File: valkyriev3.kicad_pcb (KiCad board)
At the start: 4 copper layers, 70 x 100 mm, 119 parts, among them J1 USB_C_Receptacle_USB2.0_16P, J10 Conn_01x03, J11 Conn_01x03, J2 DE9_Pins_MountingHoles, J3 SMA_180C, J4 SMA_180C, J5 Conn_01x02_Socket, J6 Conn_01x02_Socket, J7 Conn_01x02_Socket, J8 Conn_01x03, J9 Conn_01x05, Q1 BC817, Q2 BC817, Q3 BC817, Q4 BC817, Q5 BC817, Q6 DMG3420U, Q7 DMP2305U, Q8 DMG3420U, SW1 SW_SPST, SW2 SW_SPST, U1 W25Q128JVS, U10 LPS22HB, U2 ESP32-S3-MINI-1U, U3 MAX3232, U4 AMS1117-3.3, U5 TPS562202, U9 MS5607-02BA

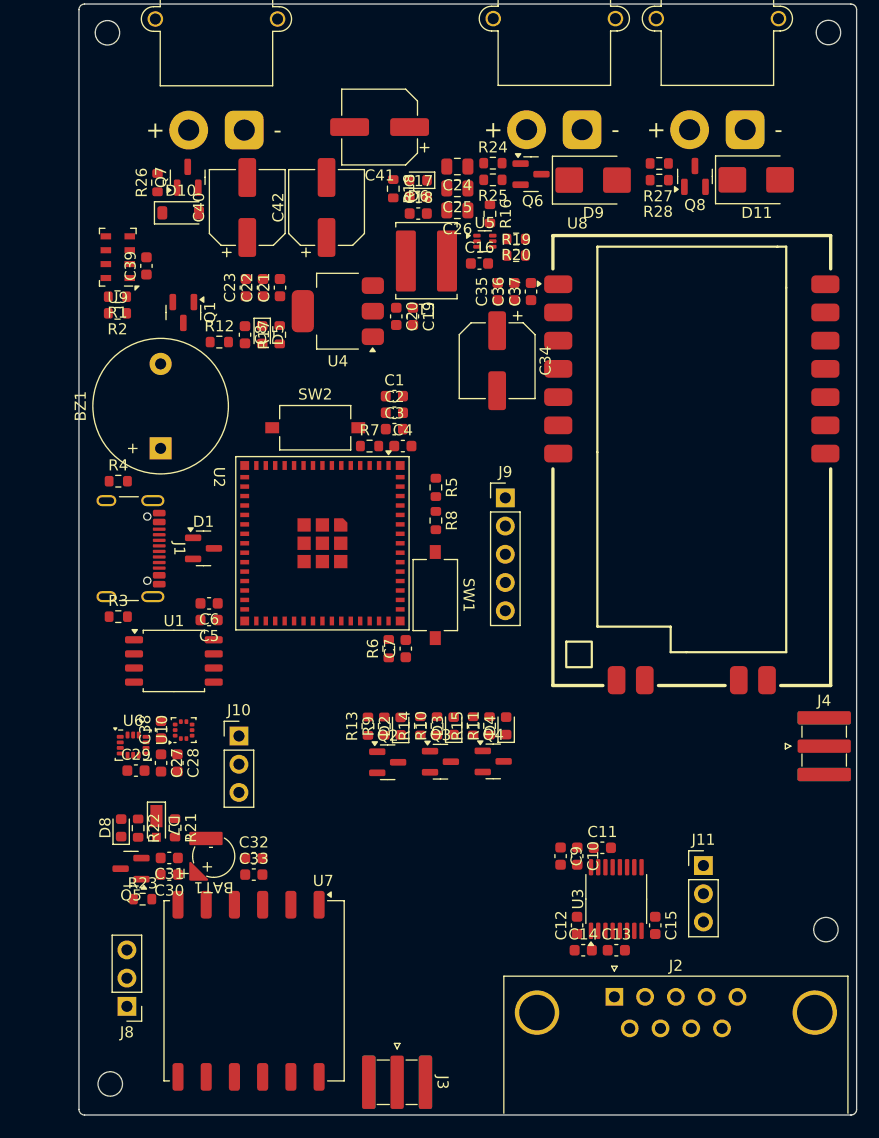
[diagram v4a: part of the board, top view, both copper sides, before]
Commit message: updated some values and routed some preliminary roads
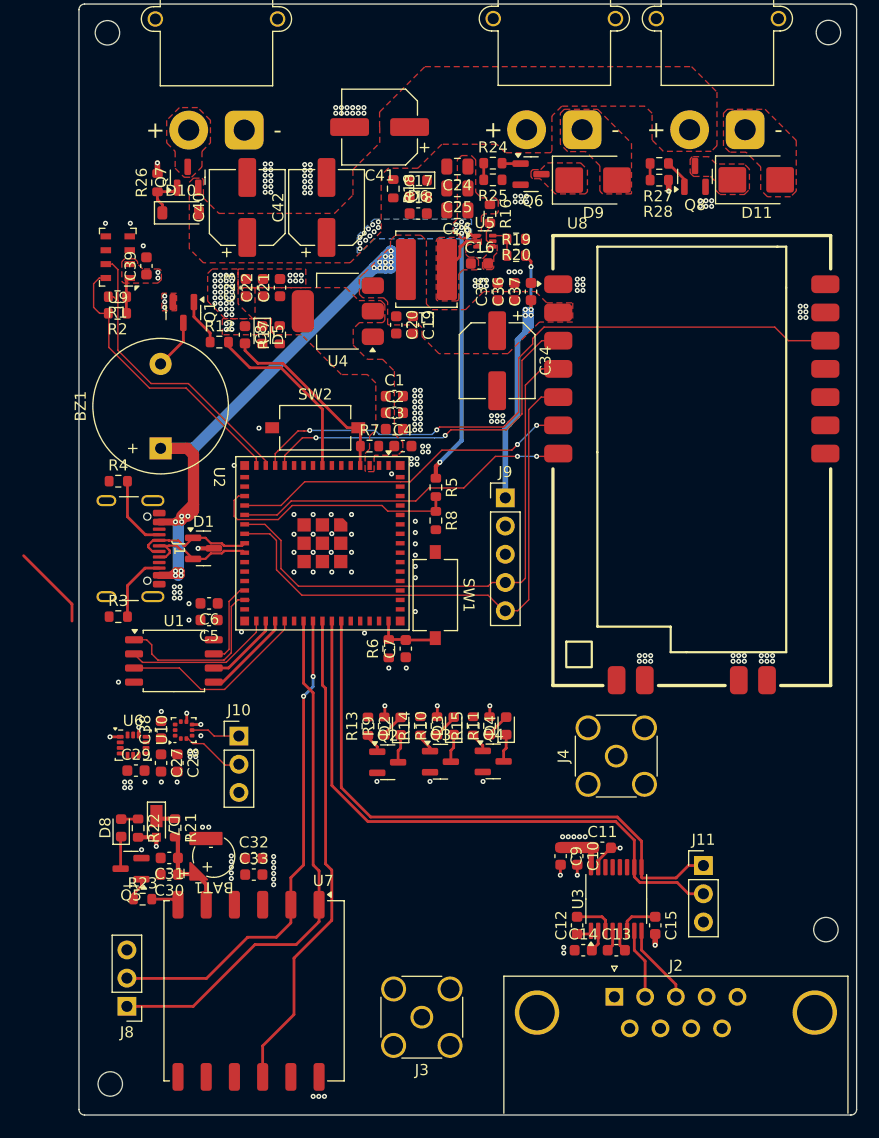
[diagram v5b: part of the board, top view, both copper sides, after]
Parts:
- J3, J4: footprint Valkyrie_footprints:SMA_180C -> Connector_Coaxial:SMA_Amphenol_132134-16_Vertical
- R8: value 54.9k -> 10k
- moved J4 18.7 mm to (146.0, 114.0), turned to 90 degrees
- moved J3 6.26 mm to (128.5, 137.5), turned to 180 degrees
- moved C19 0.76 mm to (127.7, 75.2)
- moved C20 0.76 mm to (126.2, 75.2)
- moved L1 0.76 mm to (128.9, 69.5)
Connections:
- J2 pad 5: unconnected-(J2-Pad5) -> GND
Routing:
- net +5V: track 0.00 -> 83.9 mm, vias 0 -> 23
- net LORA_RESET: track 0.00 -> 59.2 mm, vias 0 -> 2
- net ESP_TXD0: track 0.00 -> 54.2 mm
- net ESP_RXD0: track 0.00 -> 53.3 mm
- net ESP_RXD1: track 0.00 -> 50.6 mm
- net ESP_TXD1: track 0.00 -> 50.3 mm
- net ESP_TXD2: track 0.00 -> 48.1 mm
- net ESP_RXD2: track 0.00 -> 44.8 mm, vias 0 -> 2
- net GPS_RESET: track 0.00 -> 44.0 mm
- net LORA_AUX: track 0.00 -> 32.6 mm, vias 0 -> 2
- net ESP_SCL: track 0.00 -> 31.9 mm
- net ESP_SDA: track 0.00 -> 31.9 mm
- net LORA_M0: track 0.00 -> 31.2 mm, vias 0 -> 2
- net LORA_M1: track 0.00 -> 30.2 mm, vias 0 -> 2
- net VIN: track 0.00 -> 24.1 mm, vias 0 -> 19
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- added copper zone on F.Cu, net +3V3
- added copper zone on In2.Cu, net +3V3
- added copper zone on F.Cu, net +5V
- added copper zone on F.Cu, net /Connectors/DROGUE_ANODE
- added copper zone on F.Cu, net /Connectors/DROGUE_D
- added copper zone on F.Cu, net /Connectors/MAIN_ANODE
- added copper zone on F.Cu, net /Connectors/MAIN_D
- added copper zone on F.Cu, net /Power/TPS_SW
- added copper zone on F.Cu, net /Power/TPS_VBST
- added copper zone on F.Cu, net GND
- added copper zone on In1.Cu, net GND
- added copper zone on F.Cu, net VBATT
- added copper zone on B.Cu, net VIN
- added copper zone on F.Cu, net VIN

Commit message: completed routing. laid out reference designators, information and two anime girls
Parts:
- added G***: LOGO, LOGO, F.Cu at (153.0, 81.7)
- added G***: LOGO, LOGO, F.Cu at (156.1, 113.9)
- added G***: LOGO, LOGO, F.Cu at (105.0, 82.5)
- added G***: LOGO, LOGO, B.Cu at (136.0, 124.3)
- added G***: LOGO, LOGO, B.Cu at (124.9, 124.5)
- added G***: LOGO, LOGO, B.Cu at (152.6, 76.6)
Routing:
- net OUT_DROGUE: track 1.50 -> 55.5 mm, vias 0 -> 2
- net ESP_SCL: track 31.9 -> 72.5 mm, vias 0 -> 2
- net OUT_MAIN: track 1.50 -> 41.7 mm, vias 0 -> 2
- net ESP_SDA: track 31.9 -> 69.9 mm, vias 0 -> 2
- net LED_DROGUE: track 0.00 -> 30.0 mm, vias 0 -> 2
- net LED_USER: track 0.00 -> 26.7 mm, vias 0 -> 2
- net LED_MAIN: track 0.00 -> 25.2 mm, vias 0 -> 2
- net +3V3: track 16.9 -> 38.8 mm, vias 60 -> 62
- net /GPS/GPS_ANT: track 0.00 -> 15.6 mm
- net GND: track 9.34 -> 18.5 mm, vias 198 -> 363
- net +5V: track 83.9 -> 92.3 mm
- net (no net): track 7.68 -> 0.00 mm
- net /Communications/LORA_ANT: track 0.00 -> 6.85 mm
- net /Power/5V_LED: track 0.00 -> 1.49 mm
- net VIN: vias 19 -> 21
- added copper zone on B.Cu, net +5V
- added copper zone on B.Cu, net GND
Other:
- board text added: "DROGUE"
- board text added: "Drawn by Süalp K."
- board text added: "GUNALTAY ROCKET TEAM Valkyrie V3 Flight Computer"
- board text added: "GUNALTAY ROCKET TEAM Valkyrie V3 Flight Computer Drawn By: Süalp K. VIN: 7-15V DC"
- board text added: "MAIN"
- board text added: "Stack up: JLC04161H-7628"
- board text added: "VIN 7-15V DC"

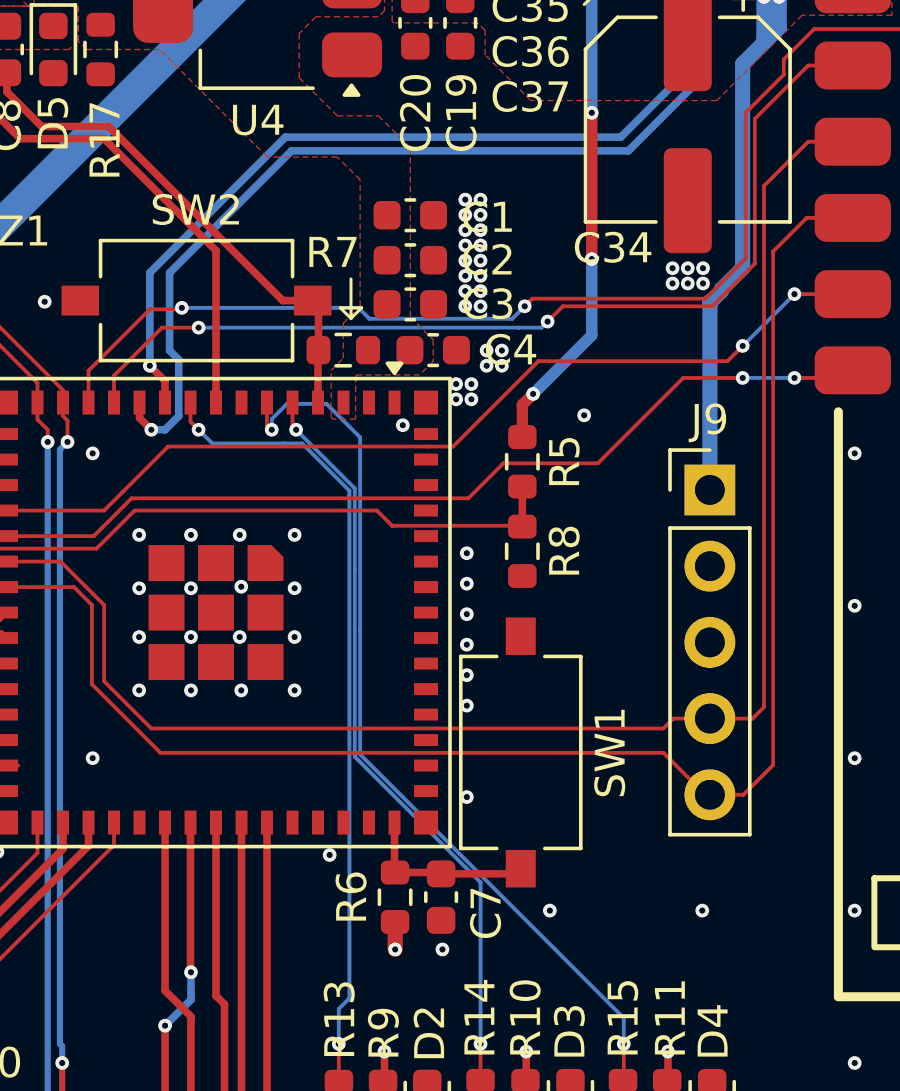
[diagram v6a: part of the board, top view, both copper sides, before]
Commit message: Added BOOT and RST labels to their respective buttons
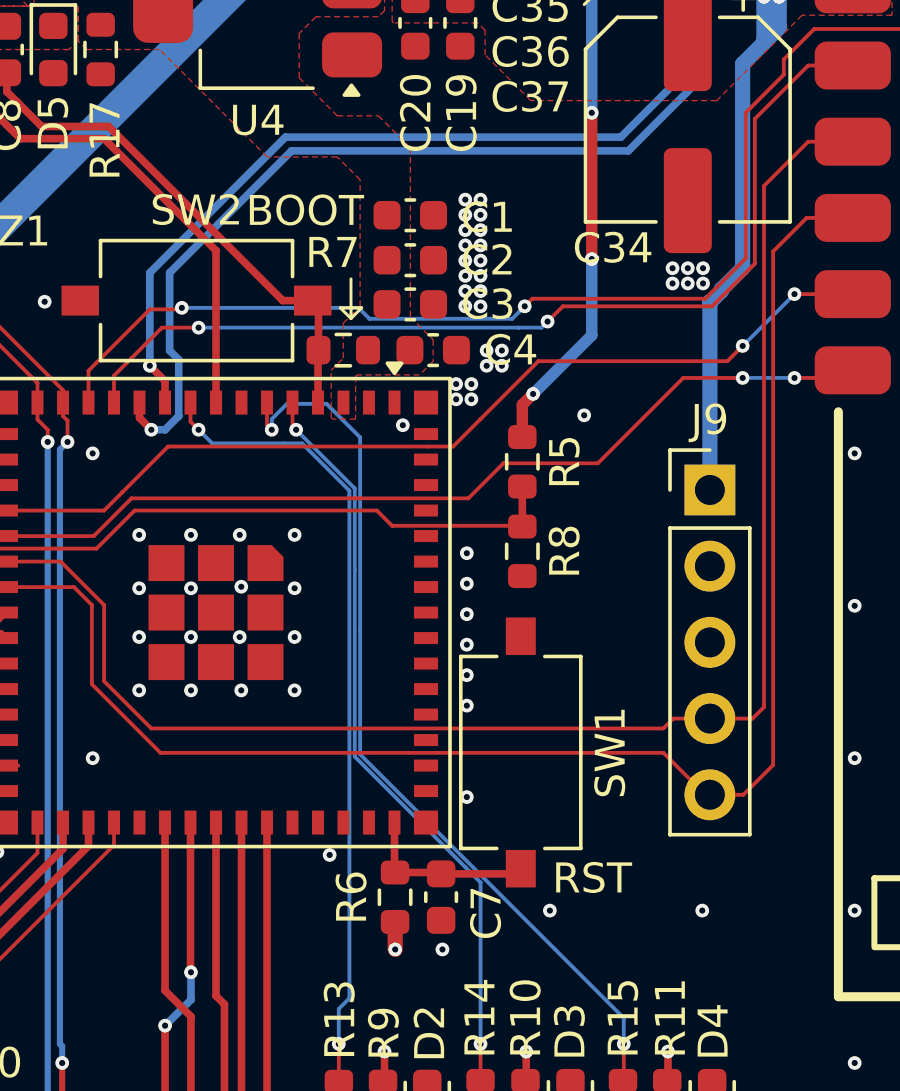
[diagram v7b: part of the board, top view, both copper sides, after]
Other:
- board text added: "BOOT"
- board text added: "RST"
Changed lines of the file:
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@@
 			(xy 118.9736 46.5328) (xy 129.9464 46.5328) (xy 130.0988 46.6852) (xy 130.0988 50.6476) (xy 130.4036 50.9524)
 			(xy 133.0452 50.9524) (xy 133.35 51.2572) (xy 133.35 53.5432) (xy 132.9944 53.8988) (xy 127.3048 53.8988)
-			(xy 127.2032 53.7972) (xy 127.2032 53.7972) (xy 126.4412 53.086) (xy 126.4412 51.6128) (xy 125.9332 51.1048)
-			(xy 119.4308 51.1048) (xy 118.7704 50.4444) (xy 118.7704 46.736)
+			(xy 127.2032 53.7972) (xy 126.4412 53.086) (xy 126.4412 51.6128) (xy 125.9332 51.1048) (xy 119.4308 51.1048)
+			(xy 118.7704 50.4444) (xy 118.7704 46.736)
 		)
 		(stroke
@@
 		)
 	)
+	(gr_text "BOOT"
+		(at 120.5484 82.042 0)
+		(layer "F.SilkS")
+		(effects
+			(font
+				(size 1 1)
+				(thickness 0.125)
+			)
+			(justify left bottom)
+		)
+	)
 	(gr_text "Stack up:\nJLC04161H-7628"
 		(at 101.6762 64.2874 90)
@@
 		(layer "F.SilkS")
 		(effects
+			(font
+				(size 1 1)
+				(thickness 0.125)
+			)
+			(justify left bottom)
+		)
+	)
+	(gr_text "RST"
+		(at 130.7592 104.2924 0)
+		(layer "F.SilkS")
+		(effects
